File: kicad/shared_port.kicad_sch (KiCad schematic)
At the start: 28 parts, among them J1 Keyboard (2x10 box), J2 SNES pad, J3 SNES pad, J4 SD (SPI), J5 PS/2 mouse, U37 SN74HC574N, U38 ATF22V10C-7PX, U39 SN74F541N

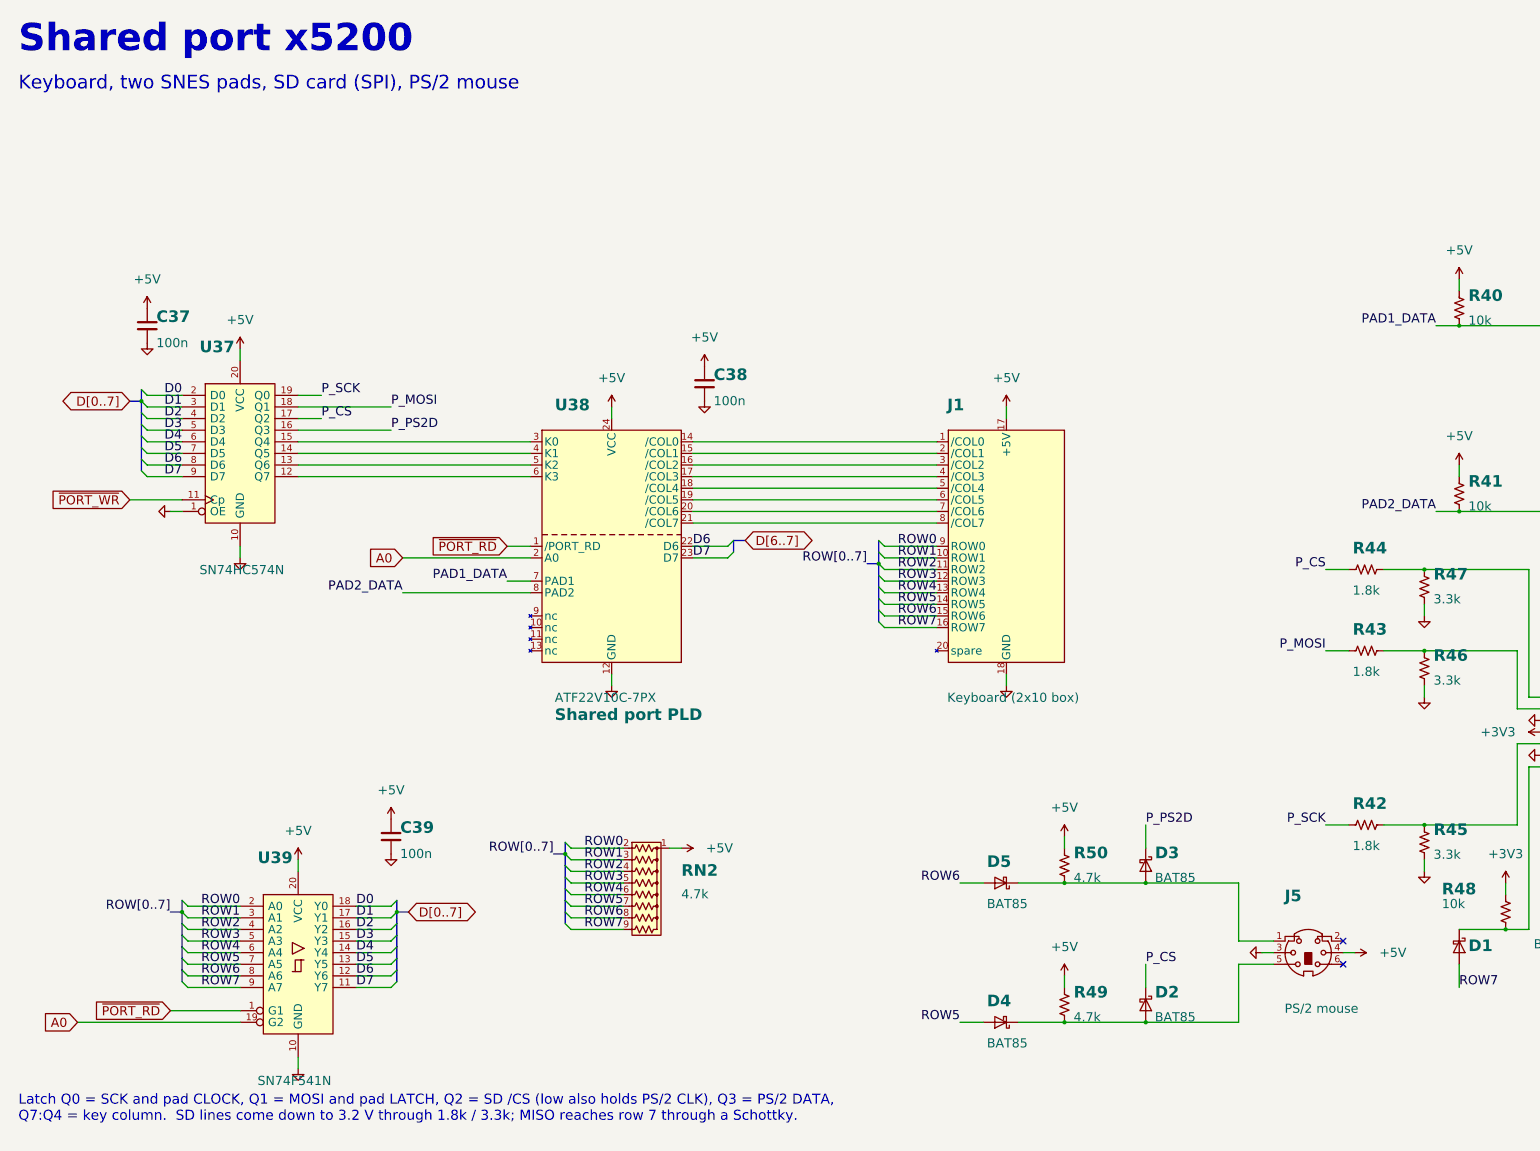
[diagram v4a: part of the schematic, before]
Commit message: Second PS/2 port: stacked dual socket, port PLD rev 02
J5 becomes a stacked dual mini-DIN 6 (Kycon KMDGX-6S/6S-S4N): mouse on
top, PS/2 keyboard below, sharing the PS/2 DATA line. No added chips:
latch Q4 (K0) holds the keyboard CLK low through D6 when no column is
driven, R55 pulls it up, and port PLD pin 9 reads it. Port PLD rev 02:
D6 on odd reads is pad 2 DATA while K0 = 0 and the keyboard CLK while
K0 = 1. VHDL model, KiCad symbols, schematic, BOM and docs updated.
Software (latch values Fx -> Ex, keyboard driver) not changed yet.

Co-Authored-By: Claude Opus 5.5 (1M context) <noreply@anthropic.com>
Claude-Session: https://claude.ai/code/session_01XntDHEWgyCnnHc7RBRvR6T
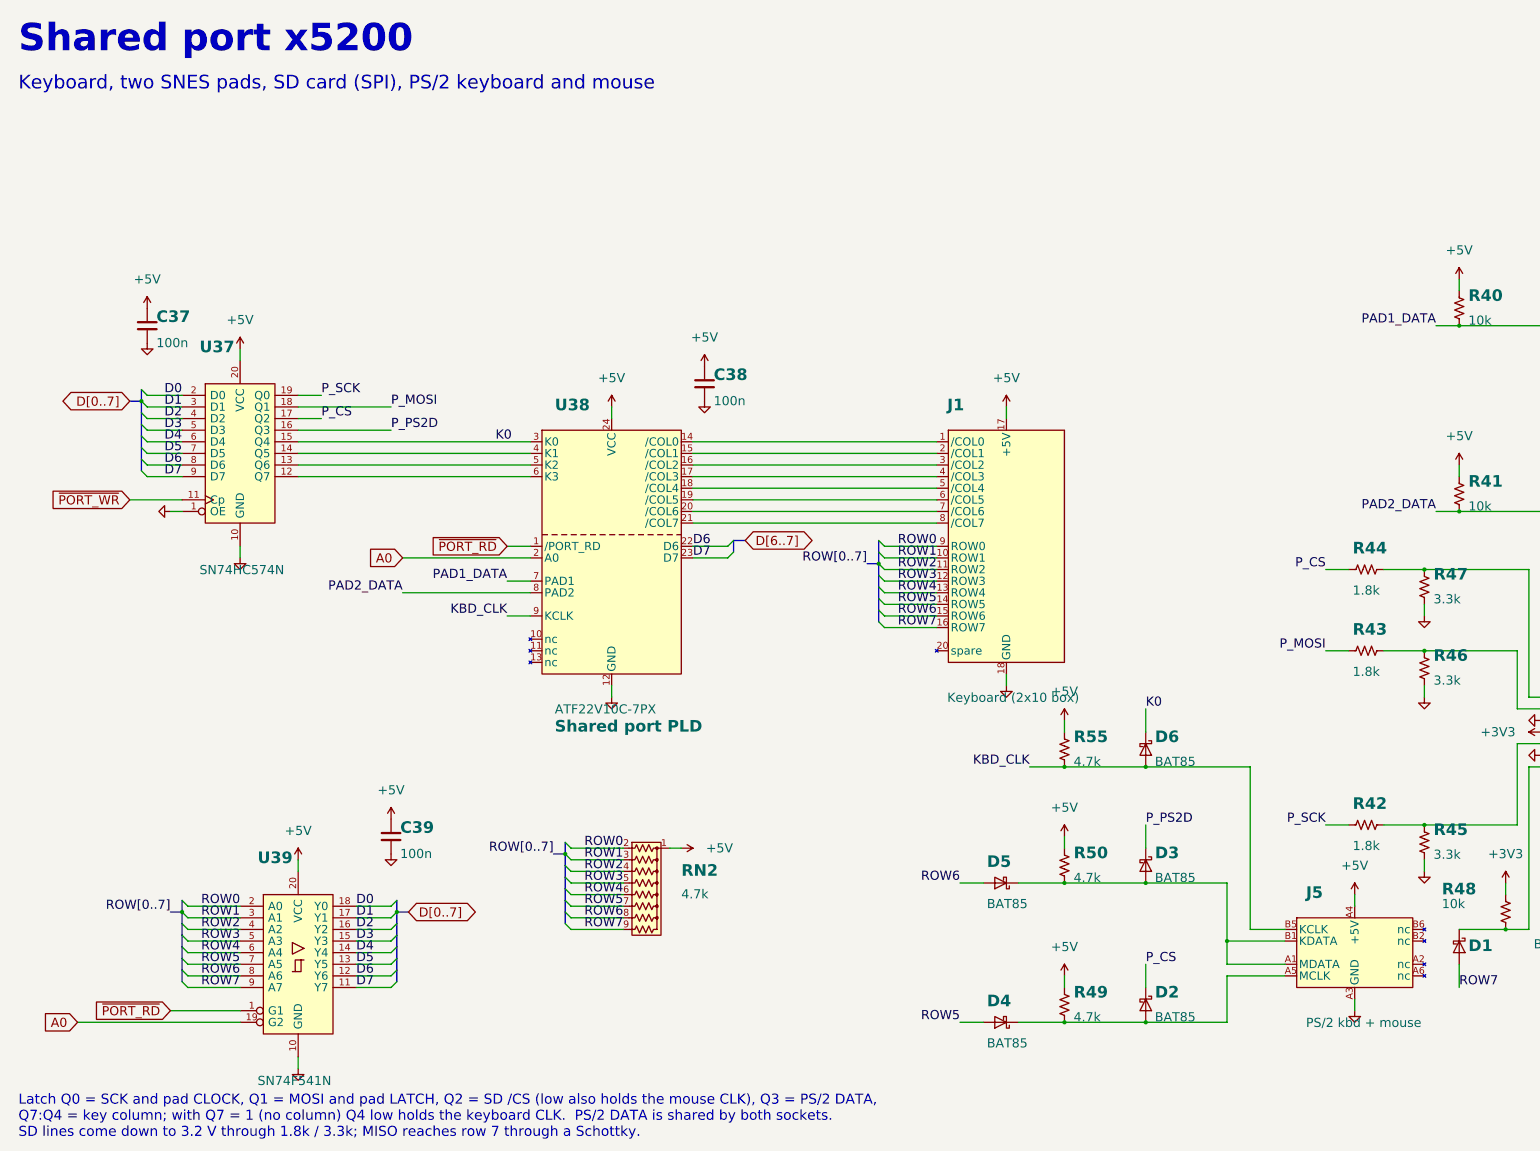
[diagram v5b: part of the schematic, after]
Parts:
- removed J5: PS/2 mouse, symbol placard_std:Mini-DIN-6
- added D6: BAT85, Diode_THT:D_DO-35_SOD27_P7.62mm_Horizontal, symbol placard_std:D_Schottky
- added J5: PS/2 kbd + mouse, symbol placard_parts:PS2_Dual_Stacked
- added R55: 4.7k, Resistor_THT:R_Axial_DIN0207_L6.3mm_D2.5mm_P10.16mm_Horizontal, symbol placard_std:R_US
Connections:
- net +5V: now also J5.A4 (+5V), J5.B4 (+5V), R55.1
- net GND: now also J5.A3 (GND), J5.B3 (GND), J5.SH (SHIELD)
- net at D3.2 (A), D5.1 (K), R50.2: now also J5.A1 (MDATA), J5.B1 (KDATA)
- net at D2.2 (A), D4.1 (K), R49.2: now also J5.A5 (MCLK)
- net K0: now reaches U37.15 (Q4), U38.3 (K0)
- net K0: now also D6.1 (K)
- net KBD_CLK: now reaches U38.9 (KCLK)
- net KBD_CLK: now also D6.2 (A), J5.B5 (KCLK), R55.2
- no-connect marks 6 -> 4
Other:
- note added: "Keyboard, two SNES pads, SD card (SPI), PS/2 keyboard and mouse"
- note added: "Latch Q0 = SCK and pad CLOCK, Q1 = MOSI and pad LATCH, Q2 = SD /CS (low also holds the mouse CLK), Q3 = PS/2 DATA,"
- note added: "Q7:Q4 = key column; with Q7 = 1 (no column) Q4 low holds the keyboard CLK. PS/2 DATA is shared by both sockets."
- note added: "SD lines come down to 3.2 V through 1.8k / 3.3k; MISO reaches row 7 through a Schottky."
- note removed: "Keyboard, two SNES pads, SD card (SPI), PS/2 mouse"
- note removed: "Latch Q0 = SCK and pad CLOCK, Q1 = MOSI and pad LATCH, Q2 = SD /CS (low also holds PS/2 CLK), Q3 = PS/2 DATA,"
- note removed: "Q7:Q4 = key column. SD lines come down to 3.2 V through 1.8k / 3.3k; MISO reaches row 7 through a Schottky."

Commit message: Main board layout: 290 x 140 mm outline, dimensions, connectors and slots placed
gen_kicad_pcb.py places the outline, dimensions, mounting holes, back-edge
I/O (USB-C, audio, VGA, PS/2), left-side SW1/SW2/SD, right-side SNES ports,
cartridge slot J8, expansion slots J9-J12 and keyboard header J1, linked to
the schematic symbols, and draws docs/placard_board_layout.png.
gen_kicad_connectors.py writes preliminary footprints for the parts KiCad
has none for; the schematic generator now assigns all connector footprints.

Co-Authored-By: Claude Opus 5.5 (1M context) <noreply@anthropic.com>
Claude-Session: https://claude.ai/code/session_013qXQudFqhMaBbYKyavQCXN
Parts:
- J2, J3: footprint (none) -> placard:SNES_Pad_Socket_Horizontal
- J4: footprint (none) -> Connector_Card:SD_Kyocera_145638009511859+
- J5: footprint (none) -> placard:PS2_Kycon_KMDGX-6S-6S-S4N

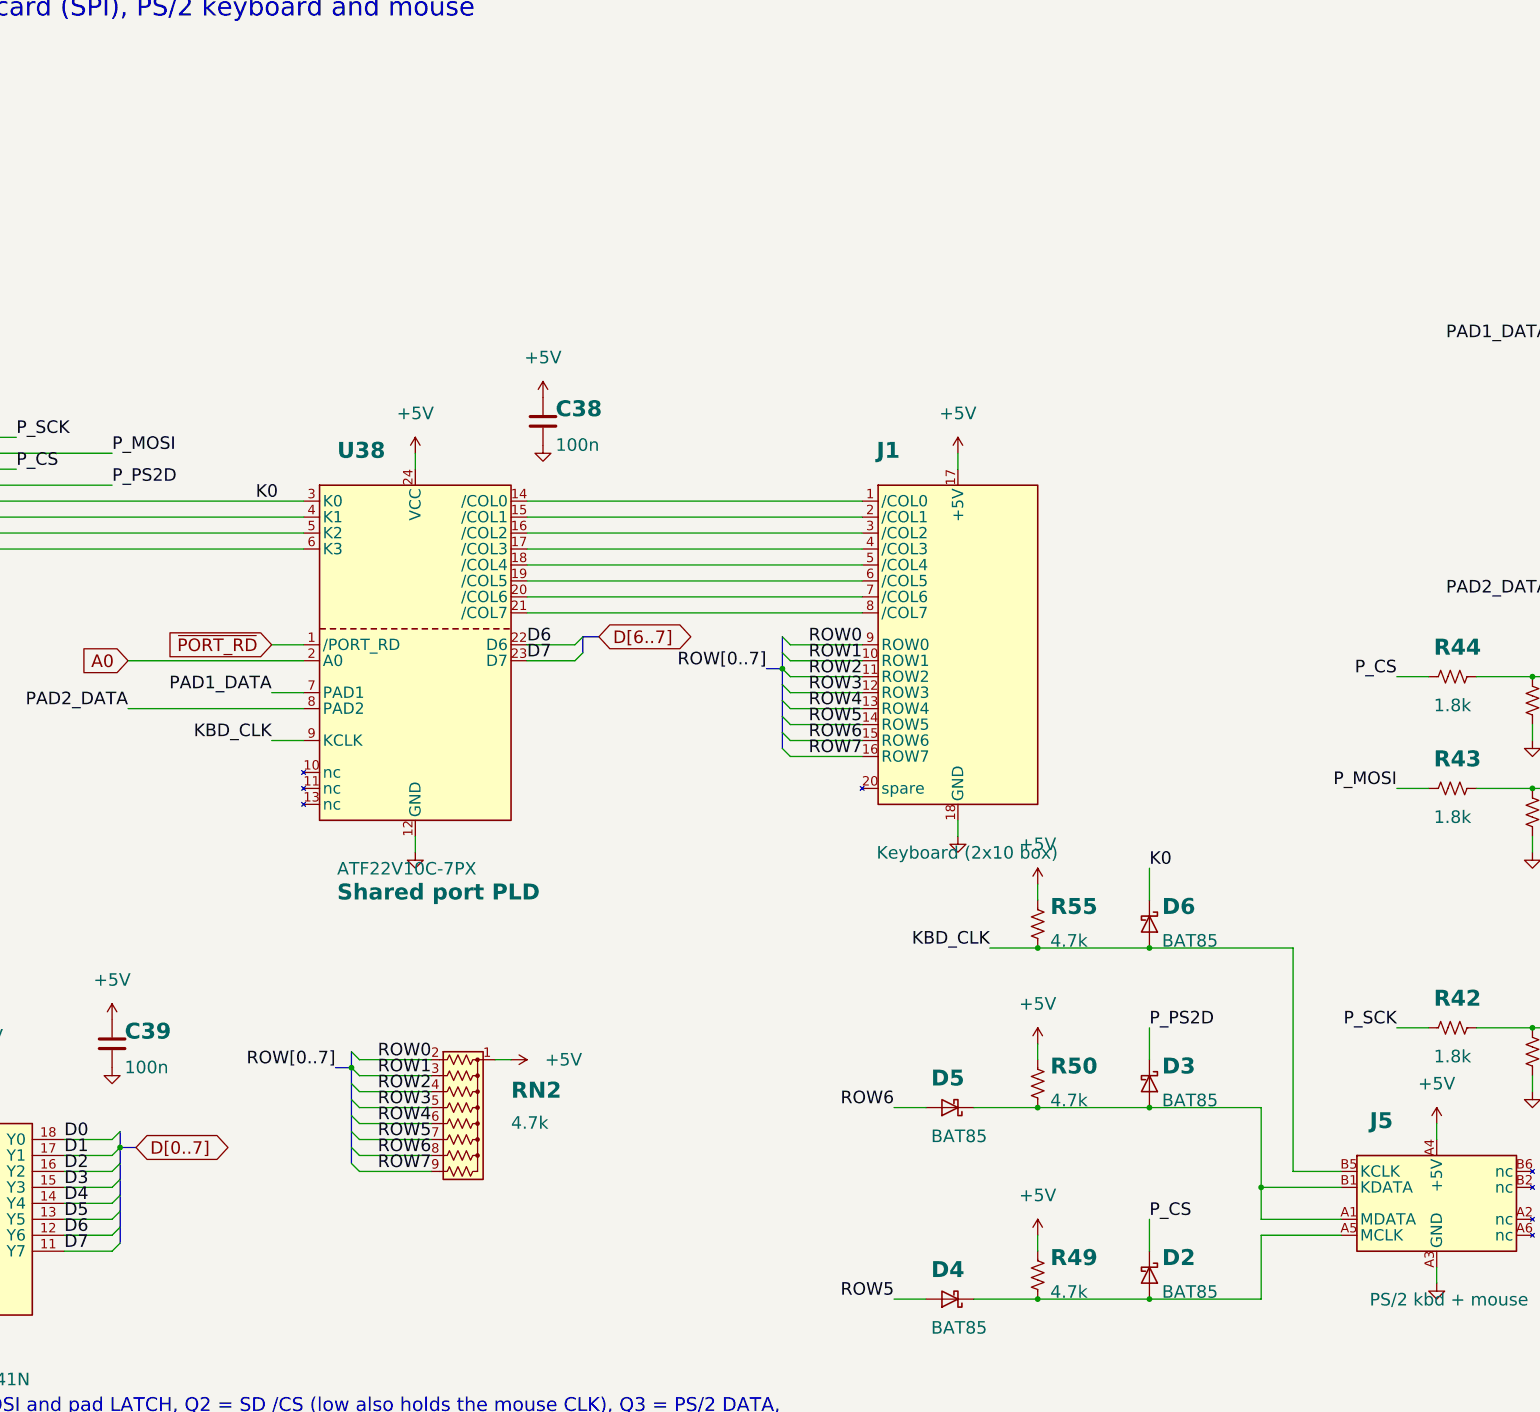
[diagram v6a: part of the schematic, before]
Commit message: Through-hole ESD clamps on external I/O; D7 TVS to through-hole SA5.0A
BAT85 steering pairs to +5V and GND on every PS/2 and SNES signal line
(D8-D21, shared port sheet) and on the VGA syncs (D22-D25, video sheet).
D7 changes from the SMD SMAJ5.0A to the DO-15 SA5.0A (through hole
wherever possible). BOM, docs and PDFs regenerated.

Co-Authored-By: Claude Opus 5.5 (1M context) <noreply@anthropic.com>
Claude-Session: https://claude.ai/code/session_01L9AkLuEg13EebxDmgXsaEp
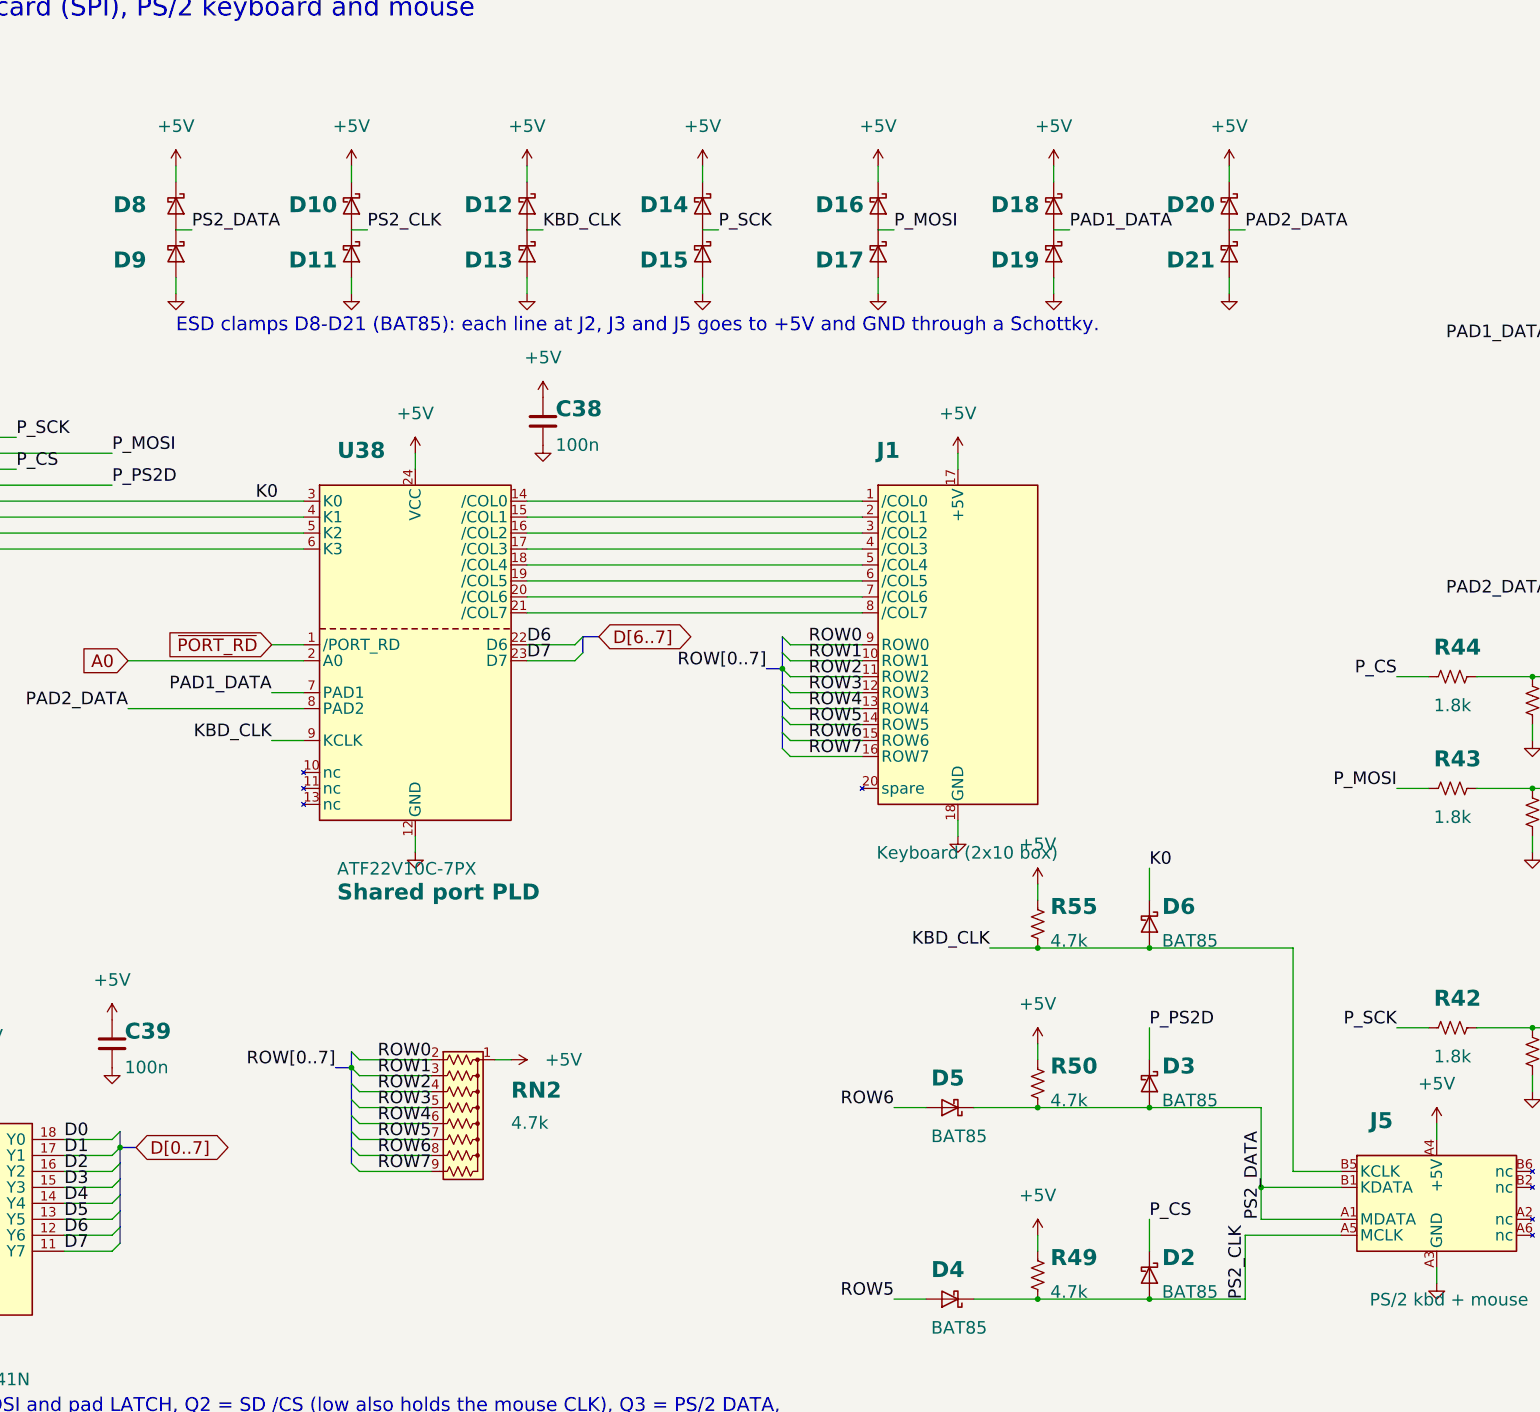
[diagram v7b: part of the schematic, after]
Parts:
- added D10, D11, D12, D13, D14, D15, D16, D17, D18, D19, D20, D21, D8, D9: BAT85, Diode_THT:D_DO-35_SOD27_P7.62mm_Horizontal, symbol placard_std:D_Schottky
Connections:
- net +5V: now also D10.1 (K), D12.1 (K), D14.1 (K), D16.1 (K), D18.1 (K), D20.1 (K), D8.1 (K)
- net GND: now also D11.2 (A), D13.2 (A), D15.2 (A), D17.2 (A), D19.2 (A), D21.2 (A), D9.2 (A)
- net KBD_CLK: now also D12.2 (A), D13.1 (K)
- net PAD1_DATA: now also D18.2 (A), D19.1 (K)
- net PAD2_DATA: now also D20.2 (A), D21.1 (K)
- net P_MOSI: now also D16.2 (A), D17.1 (K)
- net P_SCK: now also D14.2 (A), D15.1 (K)
- net PS2_DATA: now reaches D3.2 (A), D5.1 (K), J5.A1 (MDATA), J5.B1 (KDATA), R50.2
- net PS2_DATA: now also D8.2 (A), D9.1 (K)
- net PS2_CLK: now reaches D2.2 (A), D4.1 (K), J5.A5 (MCLK), R49.2
- net PS2_CLK: now also D10.2 (A), D11.1 (K)
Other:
- note added: "ESD clamps D8-D21 (BAT85): each line at J2, J3 and J5 goes to +5V and GND through a Schottky."

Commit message: Part numbers for the remaining parts; J6 Tensility 54-00174; optional J1 and J9-J12
Every schematic part gets Manufacturer/MPN: Yageo MFR-25 resistors by value,
Bourns 4609X networks, KEMET/TDK ceramics, Panasonic FR electrolytics, ECS
oscillator, Assmann VGA, Sullins headers, Wurth box header, Cherry switches.
Sockets get On Shore numbers (0.3" 24/28-pin are ED241DT/ED281DT; ED28DT is
0.6"). J6 becomes the Tensility 54-00174 TRRS jack with a footprint drawn
from its datasheet. Digi-Key prices from Justin for the oscillator, VGA and
audio jack. The expansion slot sockets and the keyboard header are optional,
with a BOM total without them.

Co-Authored-By: Claude Opus 5.5 (1M context) <noreply@anthropic.com>
Claude-Session: https://claude.ai/code/session_01L9AkLuEg13EebxDmgXsaEp
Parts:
- C37, C38, C39: MPN (none) -> C320C104K5R5TA; Manufacturer (none) -> KEMET
- J1: MPN (none) -> 61202021621; Manufacturer (none) -> Wurth Elektronik
- J4: MPN (none) -> 145638009511859+; Manufacturer (none) -> Kyocera AVX
- R40, R41, R48: MPN (none) -> MFR-25FBF52-10K; Manufacturer (none) -> Yageo
- R42, R43, R44: MPN (none) -> MFR-25FBF52-1K8; Manufacturer (none) -> Yageo
- R45, R46, R47: MPN (none) -> MFR-25FBF52-3K3; Manufacturer (none) -> Yageo
- R49, R50, R55: MPN (none) -> MFR-25FBF52-4K7; Manufacturer (none) -> Yageo
- RN2: MPN (none) -> 4609X-101-472LF; Manufacturer (none) -> Bourns
